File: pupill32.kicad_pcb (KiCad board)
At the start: 2 copper layers, 52.1 x 27.9 mm, 49 parts, among them J1 HeaderR, J2 HeaderL, J3 USB_PINS, J4 SWD_HEADER, SW1 RST_BTN, SW2 BOOT_BTN, U1 SRV05-4, U2 PY32F030F18P6, U3 CH340N, U4 AMS1117-3.3, Y1 32.768 kHz, Y2 12M

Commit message: project rename, part3
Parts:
- SW1, SW2: footprint pypill32:SW-SMD_L6.0-W3.5-LS8.2 -> pupill32:SW-SMD_L6.0-W3.5-LS8.2
- USB1: footprint pypill32:USB-C-SMD_TYPE-C-6PIN-2MD-073 -> pupill32:USB-C-SMD_TYPE-C-6PIN-2MD-073
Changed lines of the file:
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@@
 		(property ki_fp_filters "Inductor_* L_* *Ferrite*")
 		(sheetname "Root")
-		(sheetfile "pypill32.kicad_sch")
+		(sheetfile "pupill32.kicad_sch")
 		(attr smd)
 		(fp_line
@@
 		(property ki_fp_filters "SOP*3.9x4.9mm*P1.27mm*")
 		(sheetname "Root")
-		(sheetfile "pypill32.kicad_sch")
+		(sheetfile "pupill32.kicad_sch")
 		(attr smd)
 		(fp_line
@@
 		(property ki_fp_filters "Crystal*")
 		(sheetname "Root")
-		(sheetfile "pypill32.kicad_sch")
+		(sheetfile "pupill32.kicad_sch")
 		(attr through_hole)
 		(fp_line
@@
 		(property ki_fp_filters "Crystal*")
 		(sheetname "Root")
-		(sheetfile "pypill32.kicad_sch")
+		(sheetfile "pupill32.kicad_sch")
 		(attr through_hole)
 		(fp_arc
@@
 		(property ki_fp_filters "C_*")
 		(sheetname "Root")
-		(sheetfile "pypill32.kicad_sch")
+		(sheetfile "pupill32.kicad_sch")
 		(attr smd)
 		(fp_line
@@
 		(property ki_fp_filters "LED* LED_SMD:* LED_THT:*")
 		(sheetname "Root")
-		(sheetfile "pypill32.kicad_sch")
+		(sheetfile "pupill32.kicad_sch")
 		(attr smd)
 		(fp_line
@@
 		(property ki_fp_filters "C_*")
 		(sheetname "Root")
-		(sheetfile "pypill32.kicad_sch")
+		(sheetfile "pupill32.kicad_sch")
 		(attr smd)
 		(fp_line
@@
 		(property ki_fp_filters "R_*")
 		(sheetname "Root")
-		(sheetfile "pypill32.kicad_sch")
+		(sheetfile "pupill32.kicad_sch")
 		(attr smd)
 		(fp_line
@@
 		(property ki_fp_filters "MountingHole*Pad*")
 		(sheetname "Root")
-		(sheetfile "pypill32.kicad_sch")
+		(sheetfile "pupill32.kicad_sch")
 		(zone_connect 2)
 		(attr exclude_from_pos_files exclude_from_bom)
@@
 		(property ki_fp_filters "MountingHole*Pad*")
 		(sheetname "Root")
-		(sheetfile "pypill32.kicad_sch")
+		(sheetfile "pupill32.kicad_sch")
 		(zone_connect 2)
 		(attr exclude_from_pos_files exclude_from_bom)
@@
 		)
 	)
-	(footprint "pypill32:SW-SMD_L6.0-W3.5-LS8.2"
+	(footprint "pupill32:SW-SMD_L6.0-W3.5-LS8.2"
 		(layer "F.Cu")
 		(at 133.5024 85.6 90)
@@
 			)
 		)
-		(property "Footprint" "pypill32:SW-SMD_L6.0-W3.5-LS8.2"
+		(property "Footprint" "pupill32:SW-SMD_L6.0-W3.5-LS8.2"
 			(at 0 0 90)
 			(layer "F.Fab")
@@
 		)
 		(sheetname "Root")
-		(sheetfile "pypill32.kicad_sch")
+		(sheetfile "pupill32.kicad_sch")
 		(attr smd)
 		(fp_line
@@
 		(property ki_fp_filters "R_*")
 		(sheetname "Root")
-		(sheetfile "pypill32.kicad_sch")
+		(sheetfile "pupill32.kicad_sch")
 		(attr smd)
 		(fp_line
@@
 		(property ki_fp_filters "MountingHole*Pad*")
 		(sheetname "Root")
-		(sheetfile "pypill32.kicad_sch")
+		(sheetfile "pupill32.kicad_sch")
 		(zone_connect 2)
 		(attr exclude_from_pos_files exclude_from_bom)
@@
 		(property ki_fp_filters "Connector*:*_1x??_*")
 		(sheetname "Root")
-		(sheetfile "pypill32.kicad_sch")
+		(sheetfile "pupill32.kicad_sch")
 		(attr through_hole)
 		(fp_line
@@
 		(property ki_fp_filters "C_*")
 		(sheetname "Root")
-		(sheetfile "pypill32.kicad_sch")
+		(sheetfile "pupill32.kicad_sch")
 		(attr smd)
 		(fp_line
@@
 		(property ki_fp_filters "*polyfuse* *PTC*")
 		(sheetname "Root")
-		(sheetfile "pypill32.kicad_sch")
+		(sheetfile "pupill32.kicad_sch")
 		(attr smd)
 		(fp_line
@@
 		(property ki_fp_filters "R_*")
 		(sheetname "Root")
-		(sheetfile "pypill32.kicad_sch")
+		(sheetfile "pupill32.kicad_sch")
 		(attr smd)
 		(fp_line
@@
 		(property ki_fp_filters "Connector*:*_1x??_*")
 		(sheetname "Root")
-		(sheetfile "pypill32.kicad_sch")
+		(sheetfile "pupill32.kicad_sch")
 		(attr through_hole)
 		(fp_line
@@
 		(property ki_fp_filters "R_*")
 		(sheetname "Root")
-		(sheetfile "pypill32.kicad_sch")
+		(sheetfile "pupill32.kicad_sch")
 		(attr smd)
 		(fp_line
@@
 		(property ki_fp_filters "MountingHole*Pad*")
 		(sheetname "Root")
-		(sheetfile "pypill32.kicad_sch")
+		(sheetfile "pupill32.kicad_sch")
 		(zone_connect 2)
 		(attr exclude_from_pos_files exclude_from_bom)
@@
 		(property ki_fp_filters "LED* LED_SMD:* LED_THT:*")
 		(sheetname "Root")
-		(sheetfile "pypill32.kicad_sch")
+		(sheetfile "pupill32.kicad_sch")
 		(attr smd)
 		(fp_line
@@
 		)
 	)
-	(footprint "pypill32:USB-C-SMD_TYPE-C-6PIN-2MD-073"
+	(footprint "pupill32:USB-C-SMD_TYPE-C-6PIN-2MD-073"
 		(layer "F.Cu")
 		(at 94.14 75.68 -90)
@@
 			)
 		)
-		(property "Footprint" "pypill32:USB-C-SMD_TYPE-C-6PIN-2MD-073"
+		(property "Footprint" "pupill32:USB-C-SMD_TYPE-C-6PIN-2MD-073"
 			(at 0 0 90)
 			(layer "F.Fab")
@@
 		)
 		(sheetname "Root")
-		(sheetfile "pypill32.kicad_sch")
+		(sheetfile "pupill32.kicad_sch")
 		(attr smd)
 		(fp_line
@@
 			(pintype "unspecified")
 		)
-		(model "/pypill32.3dshapes/USB-C-SMD_TYPE-C-6PIN-2MD-073.wrl"
+		(model "/pupill32.3dshapes/USB-C-SMD_TYPE-C-6PIN-2MD-073.wrl"
 			(offset
 				(xyz 0 -1.2 0.9)
@@
 		(property ki_fp_filters "R_*")
 		(sheetname "Root")
-		(sheetfile "pypill32.kicad_sch")
+		(sheetfile "pupill32.kicad_sch")
 		(attr smd)
 		(fp_line
@@
 		(property ki_fp_filters "Connector*:*_1x??_*")
 		(sheetname "Root")
-		(sheetfile "pypill32.kicad_sch")
+		(sheetfile "pupill32.kicad_sch")
 		(attr through_hole)
 		(fp_line
@@
 		(property ki_fp_filters "SolderJumper*Open*")
 		(sheetname "Root")
-		(sheetfile "pypill32.kicad_sch")
+		(sheetfile "pupill32.kicad_sch")
 		(zone_connect 1)
 		(attr exclude_from_pos_files)
@@
 		(property ki_fp_filters "SOT?23*")
 		(sheetname "Root")
-		(sheetfile "pypill32.kicad_sch")
+		(sheetfile "pupill32.kicad_sch")
 		(attr smd)
 		(fp_line
@@
 		(property ki_fp_filters "Pin* Test*")
 		(sheetname "Root")
-		(sheetfile "pypill32.kicad_sch")
+		(sheetfile "pupill32.kicad_sch")
 		(attr exclude_from_pos_files)
 		(fp_circle
@@
 		(property ki_fp_filters "TSSOP*4.4x6.5mm*P0.65mm*")
 		(sheetname "Root")
-		(sheetfile "pypill32.kicad_sch")
+		(sheetfile "pupill32.kicad_sch")
 		(attr smd)
 		(fp_line
@@
 		(property ki_fp_filters "R_*")
 		(sheetname "Root")
-		(sheetfile "pypill32.kicad_sch")
+		(sheetfile "pupill32.kicad_sch")
 		(attr smd)
 		(fp_line
@@
 		(property ki_fp_filters "R_*")
 		(sheetname "Root")
-		(sheetfile "pypill32.kicad_sch")
+		(sheetfile "pupill32.kicad_sch")
 		(attr smd)
 		(fp_line
@@
 		(property ki_fp_filters "C_*")
 		(sheetname "Root")
-		(sheetfile "pypill32.kicad_sch")
+		(sheetfile "pupill32.kicad_sch")
 		(attr smd)
 		(fp_line
@@
 		(property ki_fp_filters "C_*")
 		(sheetname "Root")
-		(sheetfile "pypill32.kicad_sch")
+		(sheetfile "pupill32.kicad_sch")
 		(attr smd)
 		(fp_line
@@
 		(property ki_fp_filters "SOT?223*TabPin2*")
 		(sheetname "Root")
-		(sheetfile "pypill32.kicad_sch")
+		(sheetfile "pupill32.kicad_sch")
 		(attr smd)
 		(fp_line
@@
 		(property ki_fp_filters "Connector*:*_1x??_*")
 		(sheetname "Root")
-		(sheetfile "pypill32.kicad_sch")
+		(sheetfile "pupill32.kicad_sch")
 		(attr through_hole)
 		(fp_line
@@
 		)
 	)
-	(footprint "pypill32:SW-SMD_L6.0-W3.5-LS8.2"
+	(footprint "pupill32:SW-SMD_L6.0-W3.5-LS8.2"
 		(layer "F.Cu")
 		(at 133.1976 67.4116 -90)
@@
 			)
 		)
-		(property "Footprint" "pypill32:SW-SMD_L6.0-W3.5-LS8.2"
+		(property "Footprint" "pupill32:SW-SMD_L6.0-W3.5-LS8.2"
 			(at 0 0 -90)
 			(layer "F.Fab")
@@
 		)
 		(sheetname "Root")
-		(sheetfile "pypill32.kicad_sch")
+		(sheetfile "pupill32.kicad_sch")
 		(attr smd)
 		(fp_line
@@
 		(property ki_fp_filters "C_*")
 		(sheetname "Root")
-		(sheetfile "pypill32.kicad_sch")
+		(sheetfile "pupill32.kicad_sch")
 		(attr smd)
 		(fp_line
@@
 		(property ki_fp_filters "C_*")
 		(sheetname "Root")
-		(sheetfile "pypill32.kicad_sch")
+		(sheetfile "pupill32.kicad_sch")
 		(attr smd)
 		(fp_line
@@
 		(property ki_fp_filters "C_*")
 		(sheetname "Root")
-		(sheetfile "pypill32.kicad_sch")
+		(sheetfile "pupill32.kicad_sch")
 		(attr smd)
 		(fp_line
@@
 		(property ki_fp_filters "C_*")
 		(sheetname "Root")
-		(sheetfile "pypill32.kicad_sch")
+		(sheetfile "pupill32.kicad_sch")
 		(attr smd)
 		(fp_line
@@
 		(property ki_fp_filters "C_*")
 		(sheetname "Root")
-		(sheetfile "pypill32.kicad_sch")
+		(sheetfile "pupill32.kicad_sch")
 		(attr smd)
 		(fp_line
@@
 		(property ki_fp_filters "C_*")
 		(sheetname "Root")
-		(sheetfile "pypill32.kicad_sch")
+		(sheetfile "pupill32.kicad_sch")
 		(attr smd)
 		(fp_line
@@
 		(property ki_fp_filters "C_*")
 		(sheetname "Root")
-		(sheetfile "pypill32.kicad_sch")
+		(sheetfile "pupill32.kicad_sch")
 		(attr smd)
 		(fp_line
@@
 		(property ki_fp_filters "C_*")
 		(sheetname "Root")
-		(sheetfile "pypill32.kicad_sch")
+		(sheetfile "pupill32.kicad_sch")
 		(attr smd)
 		(fp_line
@@
 		(property ki_fp_filters "C_*")
 		(sheetname "Root")
-		(sheetfile "pypill32.kicad_sch")
+		(sheetfile "pupill32.kicad_sch")
 		(attr smd)
 		(fp_line
@@
 		(property ki_fp_filters "C_*")
 		(sheetname "Root")
-		(sheetfile "pypill32.kicad_sch")
+		(sheetfile "pupill32.kicad_sch")
 		(attr smd)
 		(fp_line
@@
 		(property ki_fp_filters "C_*")
 		(sheetname "Root")
-		(sheetfile "pypill32.kicad_sch")
+		(sheetfile "pupill32.kicad_sch")
 		(attr smd)
 		(fp_line
@@
 		(property ki_fp_filters "C_*")
 		(sheetname "Root")
-		(sheetfile "pypill32.kicad_sch")
+		(sheetfile "pupill32.kicad_sch")
 		(attr smd)
 		(fp_line
@@
 		(property ki_fp_filters "C_*")
 		(sheetname "Root")
-		(sheetfile "pypill32.kicad_sch")
+		(sheetfile "pupill32.kicad_sch")
 		(attr smd)
 		(fp_line

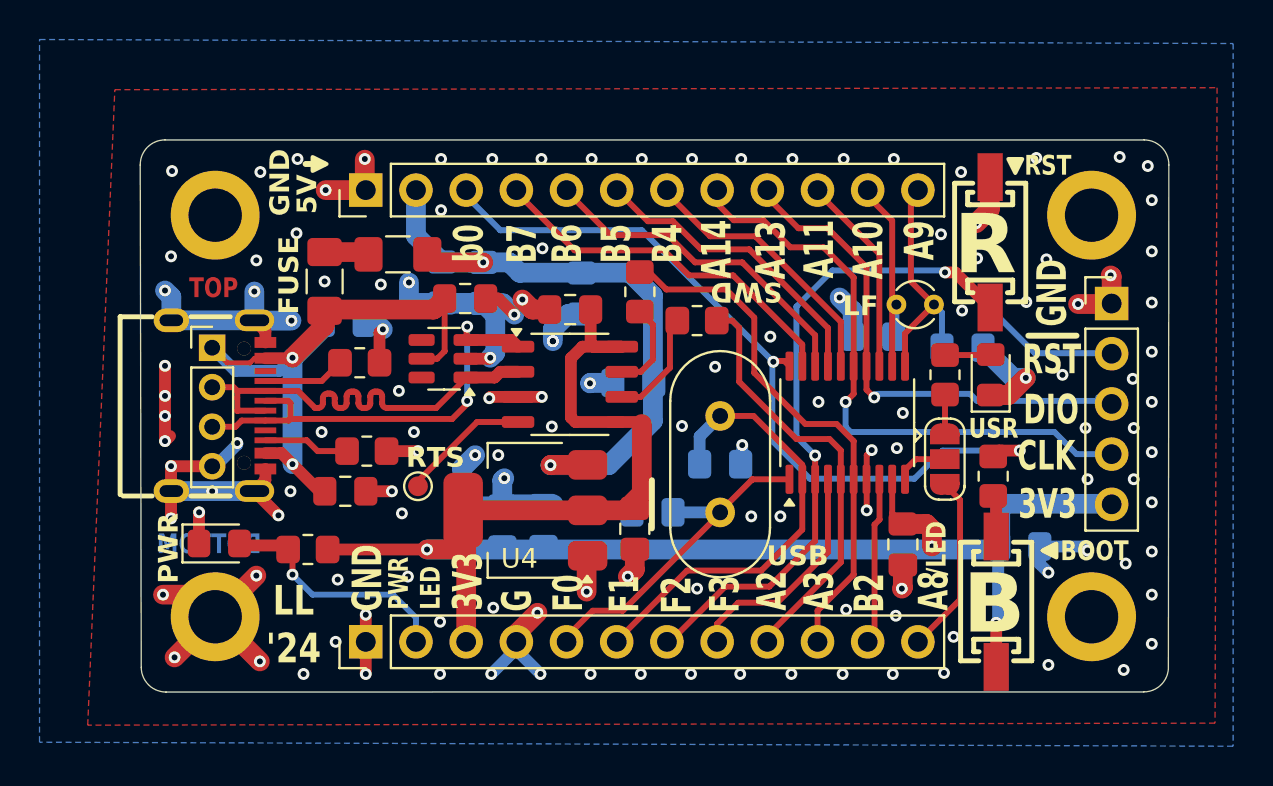
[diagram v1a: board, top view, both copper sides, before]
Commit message: revA errata -> revB
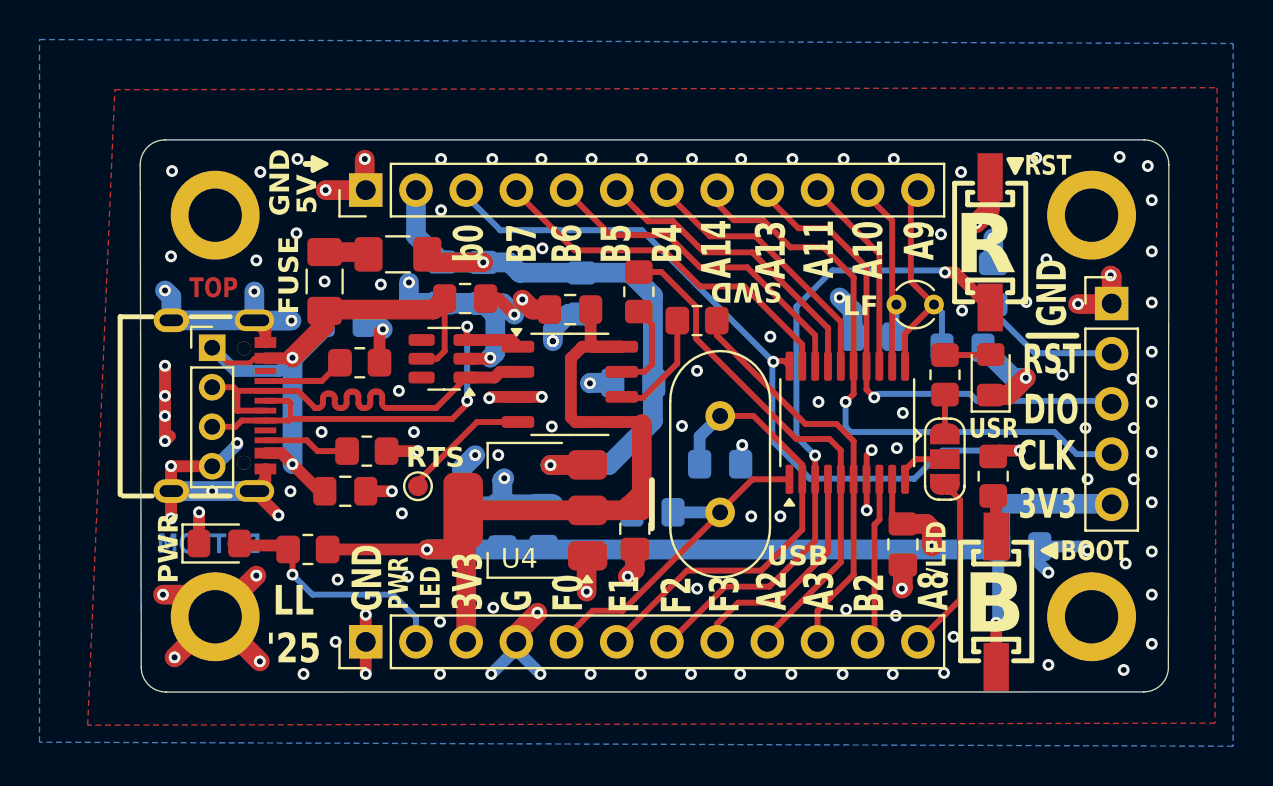
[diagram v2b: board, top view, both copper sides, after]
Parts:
- added C19: 100nF, Capacitor_SMD:C_0805_2012Metric_Pad1.18x1.45mm_HandSolder, B.Cu at (133.3, 69.5)
- R2: value 1k -> 5k1
- moved R5 0.05 mm to (115.4, 69.9)
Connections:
- R5 pad 2: PYURX -> PYUTX
- R6 pad 2: PYUTX -> PYURX
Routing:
- net PYURX: track 26.9 -> 20.8 mm
- net PYUTX: track 21.8 -> 26.1 mm
- net GND: track 124.2 -> 125.5 mm
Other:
- board text added: "LL '25"
- board text added: "rev.B"
- board text removed: "LL '24"
- board text removed: "rev.A"

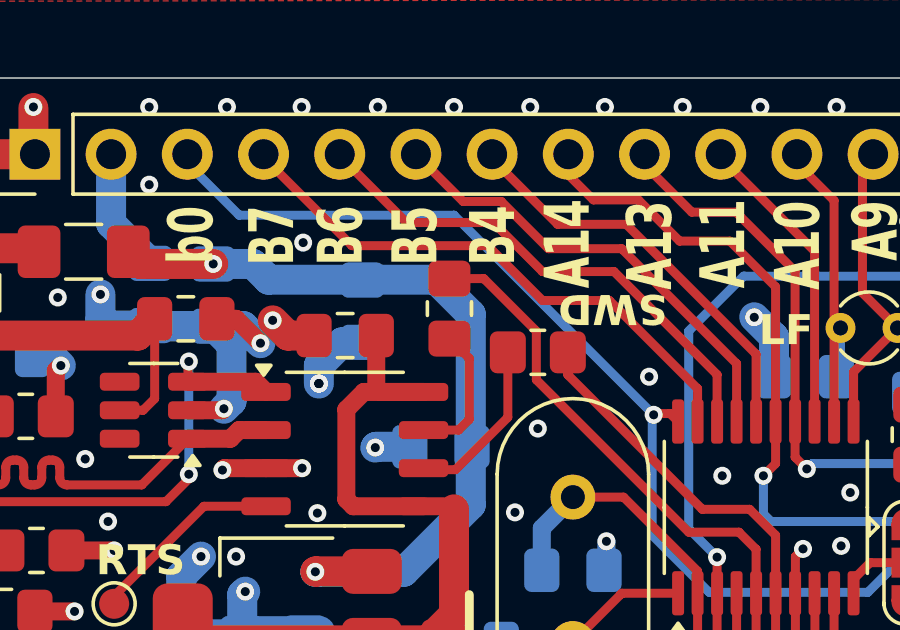
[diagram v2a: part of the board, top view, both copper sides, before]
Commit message: R1 boot0 pulldown
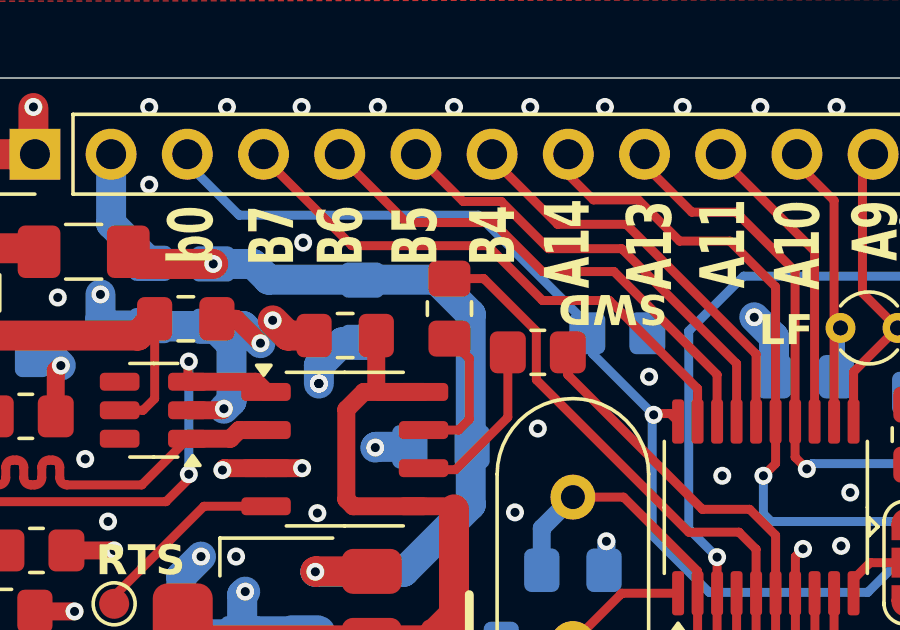
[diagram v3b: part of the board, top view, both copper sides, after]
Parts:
- added R1: 10k, Resistor_SMD:R_0805_2012Metric_Pad1.20x1.40mm_HandSolder, B.Cu at (121.0, 70.7)
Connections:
- C9 pad 1: VBUS -> unconnected-(C9-Pad1)
- C9 pad 2: GND -> unconnected-(C9-Pad2)
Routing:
- net GND: track 125.5 -> 124.2 mm
- net unconnected-(C9-Pad2): track 0.00 -> 1.32 mm
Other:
- board text removed: "A13=SWDIO"
- board text removed: "A14=SWCLK"

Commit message: tantalum
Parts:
- removed C16: 10uF, Capacitor_SMD:C_0805_2012Metric_Pad1.18x1.45mm_HandSolder
- removed C2: 1uF, Capacitor_SMD:C_0805_2012Metric_Pad1.18x1.45mm_HandSolder
- added C20: 22uF, Capacitor_Tantalum_SMD:CP_EIA-3528-21_Kemet-B_Pad1.50x2.35mm_HandSolder, B.Cu at (107.7, 81.5)
- moved C5 2.34 mm to (110.8, 81.9)
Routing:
- net GND: track 124.2 -> 126.2 mm, vias 133 -> 132
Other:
- board text added: "LICENSE: CERN- OHL-W"
- board text added: "PCB rev.B"
- board text removed: "CERN-OHL-W"
- board text removed: "rev.B"

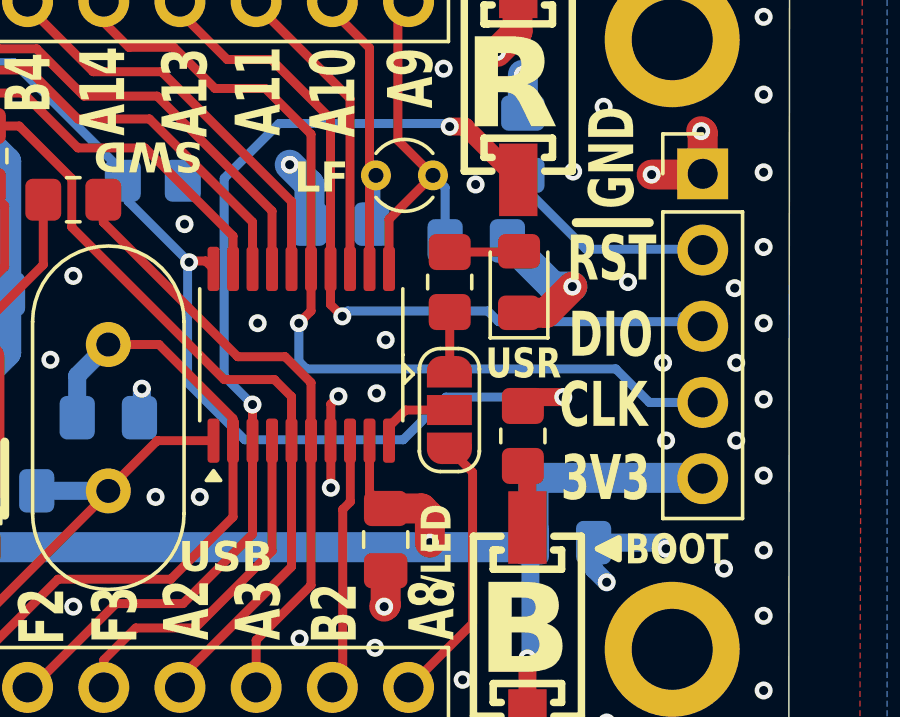
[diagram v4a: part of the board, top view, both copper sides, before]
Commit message: SWD resistors, changelog update
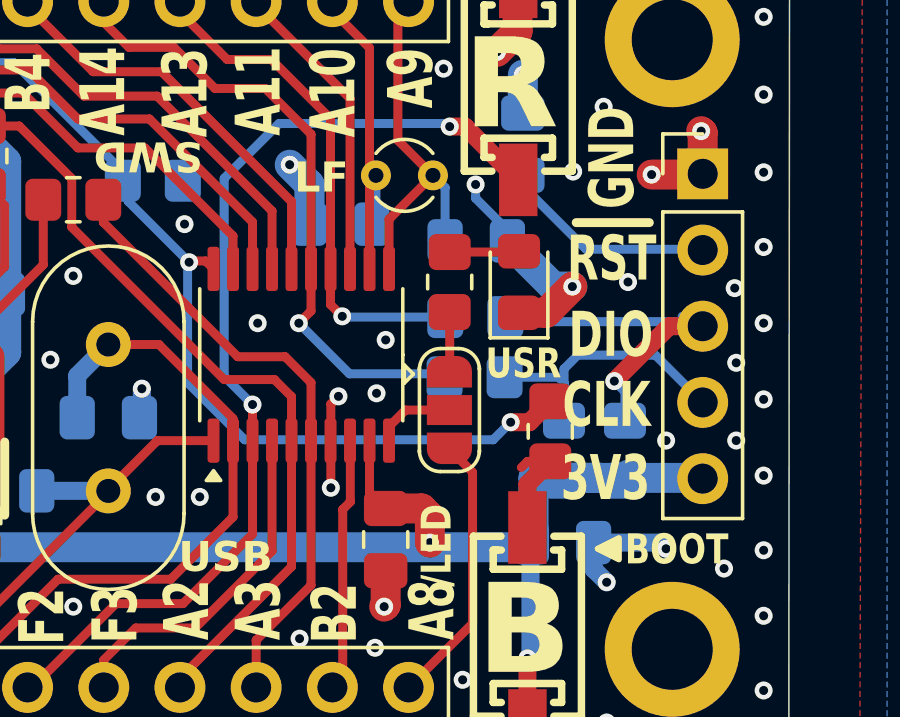
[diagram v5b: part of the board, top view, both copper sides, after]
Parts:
- added R10: 22R, Resistor_SMD:R_0805_2012Metric_Pad1.20x1.40mm_HandSolder, B.Cu at (131.8, 75.3)
- added R11: 10k, Resistor_SMD:R_0805_2012Metric_Pad1.20x1.40mm_HandSolder, B.Cu at (134.7, 79.7)
- added R12: 10k, Resistor_SMD:R_0805_2012Metric_Pad1.20x1.40mm_HandSolder, B.Cu at (136.8, 79.7)
- added R9: 22R, Resistor_SMD:R_0805_2012Metric_Pad1.20x1.40mm_HandSolder, B.Cu at (131.7, 77.3)
- moved R8 0.93 mm to (134.3, 79.1)
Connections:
- J1 pad 8: SWDCLK -> /PA14
- J1 pad 9: SWDIO -> /PA13
- U2 pad 14: SWDIO -> /PA13
- U2 pad 15: SWDCLK -> /PA14
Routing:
- net /PA14: track 0.00 -> 21.2 mm, vias 0 -> 1
- net SWDCLK: track 30.9 -> 10.5 mm, vias 1 -> 0
- net /PA13: track 0.00 -> 17.0 mm, vias 0 -> 1
- net SWDIO: track 25.9 -> 11.9 mm
- net GND: track 126.2 -> 128.5 mm, vias 132 -> 131
- net BOOT0: track 40.3 -> 38.4 mm
- net +3V3: track 85.0 -> 86.4 mm
- net Net-(R8-Pad1): track 2.19 -> 3.57 mm
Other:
- board text added: "PY32F030 F18P6"
- board text removed: "MCU: PY32F030 F18P6"
- board text removed: "SWCLK"
- board text removed: "SWDIO"
